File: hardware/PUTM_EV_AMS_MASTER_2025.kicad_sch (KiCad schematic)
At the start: 42 parts, among them IC11 ISO6760, IC7 ISO6760, IC8 3.3V/0.5A, J1 M80-5100642, J10 M300-MV10345M1, J12 M80-51034XX, J2 USB_C_Receptacle_USB2.0_14P, J3 M80-51014XX, J4 FTSH-107-01-L-D-K, J5 M80-51004XX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

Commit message: layotu done, some more routing done
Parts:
- removed TP1: TestPoint_Small, TestPoint:TestPoint_THTPad_D1.0mm_Drill0.5mm, symbol Connector:TestPoint_Small
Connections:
- net Isolated ADC/CAR_I: now also J8.2 (Pin_2); no longer J8.1 (Pin_1)
- net Isolated ADC/CAR_I_REF: now also J8.1 (Pin_1); no longer J8.2 (Pin_2)
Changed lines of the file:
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@@
 	)
 	(symbol
-		(lib_id "Connector:TestPoint_Small")
-		(at 45.72 54.61 0)
-		(unit 1)
-		(exclude_from_sim no)
-		(in_bom yes)
-		(on_board yes)
-		(dnp no)
-		(property "Reference" "TP1"
-			(at 43.18 54.61 0)
-			(effects
-				(font
-					(size 1.27 1.27)
-				)
-				(justify right)
-			)
-		)
-		(property "Value" "TestPoint_Small"
-			(at 46.99 55.8799 0)
-			(effects
-				(font
-					(size 1.27 1.27)
-				)
-				(justify left)
-				(hide yes)
-			)
-		)
-		(property "Footprint" "TestPoint:TestPoint_THTPad_D1.0mm_Drill0.5mm"
-			(at 50.8 54.61 0)
-			(effects
-				(font
-					(size 1.27 1.27)
-				)
-				(hide yes)
-			)
-		)
-		(property "Datasheet" "~"
-			(at 50.8 54.61 0)
-			(effects
-				(font
-					(size 1.27 1.27)
-				)
-				(hide yes)
-			)
-		)
-		(property "Description" "test point"
-			(at 45.72 54.61 0)
-			(effects
-				(font
-					(size 1.27 1.27)
-				)
-				(hide yes)
-			)
-		)
-		(pin "1"
-		)
-		(instances
-			(project ""
-				(path "/b456cffc-d9d7-4c91-91f2-36ec9a65dd1b"
-					(reference "TP1")
-					(unit 1)
-				)
-			)
-		)
-	)
-	(symbol
 		(lib_name "GND_28")
 		(lib_id "power:GND")
@@
 		)
 		(pin "CAR_I" input
-			(at 74.93 133.35 180)
+			(at 74.93 135.89 180)
 			(effects
 				(font
@@
 		)
 		(pin "CAR_I_REF" input
-			(at 74.93 135.89 180)
+			(at 74.93 133.35 180)
 			(effects
 				(font

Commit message: routing done, drc checked
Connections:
- net AIR_P_DETECTION: now also J12.21 (Pin_21); no longer J12.24 (Pin_24)
- net EXT_MOSI: now also J12.12 (Pin_12); no longer J12.13 (Pin_13)
- net EXT_SCK: now also J12.13 (Pin_13); no longer J12.12 (Pin_12)
- net GND: now also J12.2 (Pin_2)
- net TSMS: no longer J12.18 (Pin_18)
- no-connect marks 23 -> 21

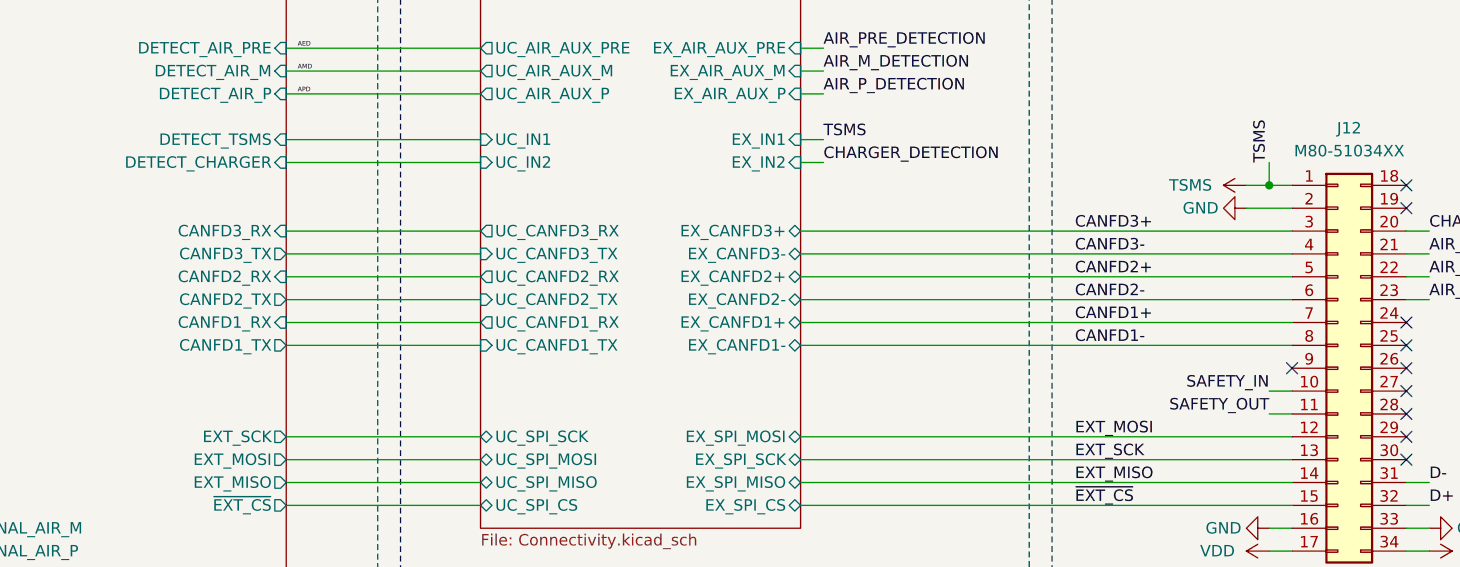
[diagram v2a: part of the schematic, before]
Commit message: changing mcu done + new routing
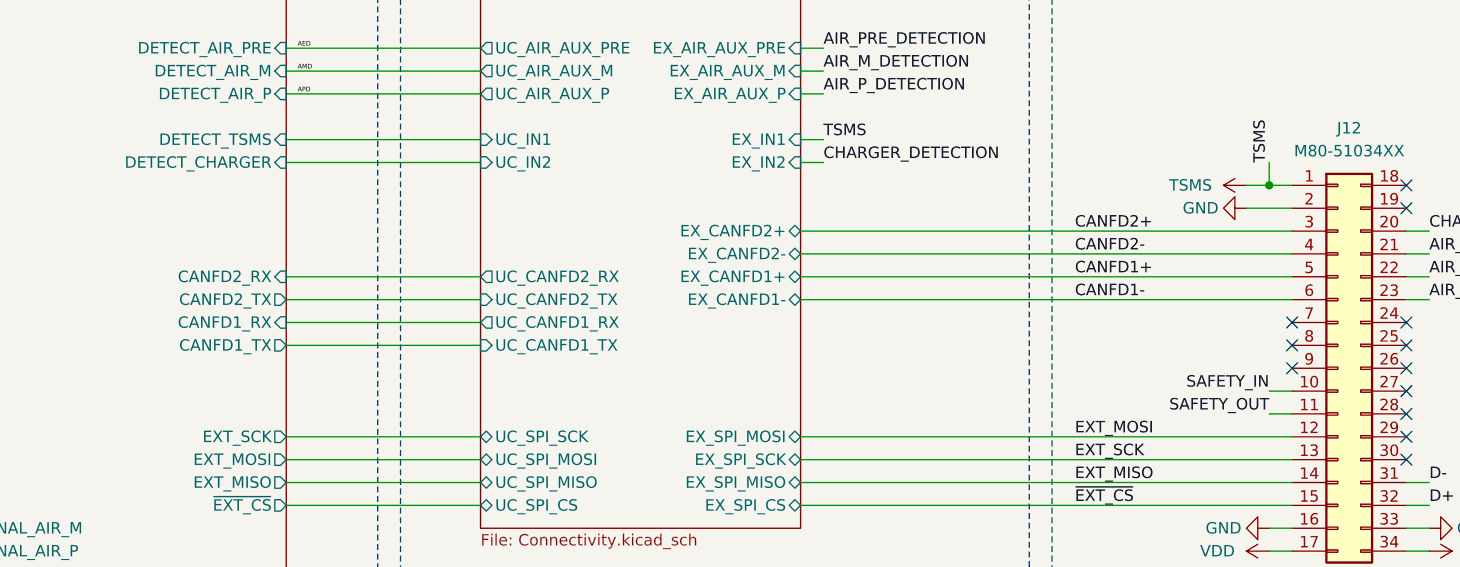
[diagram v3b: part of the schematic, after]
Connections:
- net CANFD3+ is gone; now on net CANFD2+: J12.3 (Pin_3)
- net CANFD3- is gone; now on net CANFD2-: J12.4 (Pin_4)
- net CANFD1+: now also J12.5 (Pin_5); no longer J12.7 (Pin_7)
- net CANFD1-: now also J12.6 (Pin_6); no longer J12.8 (Pin_8)
- net CANFD2+: no longer J12.5 (Pin_5)
- net CANFD2-: no longer J12.6 (Pin_6)
- no-connect marks 21 -> 23
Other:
- sheet Connectivity ports: added none; removed EX_CANFD3+, EX_CANFD3-, UC_CANFD3_RX, UC_CANFD3_TX
- sheet MCU ports: added none; removed CANFD3_RX, CANFD3_TX
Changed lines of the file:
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@@
 	)
 	(no_connect
+		(at 361.95 210.82)
+	)
+	(no_connect
+		(at 361.95 213.36)
+	)
+	(no_connect
 		(at 361.95 215.9)
 	)
@@
 	(wire
 		(pts
+			(xy 307.34 208.28) (xy 361.95 208.28)
+		)
+		(stroke
+			(width 0)
+			(type default)
+		)
+	)
+	(wire
+		(pts
 			(xy 250.19 106.68) (xy 327.66 106.68)
 		)
@@
 	(wire
 		(pts
+			(xy 307.34 200.66) (xy 361.95 200.66)
+		)
+		(stroke
+			(width 0)
+			(type default)
+		)
+	)
+	(wire
+		(pts
 			(xy 38.1 262.89) (xy 35.56 262.89)
 		)
@@
 	(wire
 		(pts
+			(xy 307.34 205.74) (xy 361.95 205.74)
+		)
+		(stroke
+			(width 0)
+			(type default)
+		)
+	)
+	(wire
+		(pts
 			(xy 114.3 238.76) (xy 114.3 267.97)
 		)
@@
 	(wire
 		(pts
-			(xy 307.34 210.82) (xy 361.95 210.82)
-		)
-		(stroke
-			(width 0)
-			(type default)
-		)
-	)
-	(wire
-		(pts
 			(xy 208.28 81.28) (xy 213.36 81.28)
 		)
@@
 	(wire
 		(pts
-			(xy 307.34 208.28) (xy 361.95 208.28)
-		)
-		(stroke
-			(width 0)
-			(type default)
-		)
-	)
-	(wire
-		(pts
 			(xy 250.19 93.98) (xy 375.92 93.98)
 		)
@@
 	(wire
 		(pts
-			(xy 307.34 205.74) (xy 361.95 205.74)
-		)
-		(stroke
-			(width 0)
-			(type default)
-		)
-	)
-	(wire
-		(pts
 			(xy 179.07 62.23) (xy 181.61 62.23)
 		)
@@
 		)
 	)
-	(wire
-		(pts
-			(xy 250.19 203.2) (xy 271.78 203.2)
-		)
-		(stroke
-			(width 0)
-			(type default)
-		)
-	)
 	(polyline
 		(pts
@@
 	(wire
 		(pts
-			(xy 307.34 200.66) (xy 361.95 200.66)
-		)
-		(stroke
-			(width 0)
-			(type default)
-		)
-	)
-	(wire
-		(pts
 			(xy 250.19 99.06) (xy 267.97 99.06)
 		)
@@
 		)
 	)
-	(wire
-		(pts
-			(xy 307.34 203.2) (xy 361.95 203.2)
-		)
-		(stroke
-			(width 0)
-			(type default)
-		)
-	)
 	(polyline
 		(pts
@@
 	(wire
 		(pts
-			(xy 48.26 114.3) (xy 74.93 114.3)
+			(xy 307.34 203.2) (xy 361.95 203.2)
 		)
 		(stroke
@@
 	(wire
 		(pts
-			(xy 107.95 172.72) (xy 125.73 172.72)
+			(xy 48.26 114.3) (xy 74.93 114.3)
 		)
 		(stroke
@@
 	(wire
 		(pts
-			(xy 392.43 31.75) (xy 392.43 39.37)
+			(xy 107.95 172.72) (xy 125.73 172.72)
 		)
 		(stroke
@@
 	(wire
 		(pts
-			(xy 85.09 41.91) (xy 85.09 44.45)
+			(xy 392.43 31.75) (xy 392.43 39.37)
 		)
 		(stroke
@@
 	(wire
 		(pts
-			(xy 307.34 226.06) (xy 361.95 226.06)
+			(xy 85.09 41.91) (xy 85.09 44.45)
 		)
 		(stroke
@@
 	(wire
 		(pts
-			(xy 85.09 52.07) (xy 85.09 54.61)
+			(xy 307.34 226.06) (xy 361.95 226.06)
 		)
 		(stroke
@@
 	(wire
 		(pts
-			(xy 250.19 200.66) (xy 271.78 200.66)
+			(xy 85.09 52.07) (xy 85.09 54.61)
 		)
 		(stroke
@@
 		)
 	)
-	(wire
-		(pts
-			(xy 307.34 213.36) (xy 361.95 213.36)
-		)
-		(stroke
-			(width 0)
-			(type default)
-		)
-	)
 	(rectangle
 		(start 157.48 242.57)
@@
 	)
 	(label "CANFD2-"
-		(at 337.82 208.28 0)
+		(at 337.82 203.2 0)
 		(fields_autoplaced yes)
 		(effects
@@
 		)
 	)
-	(label "CANFD3+"
-		(at 337.82 200.66 0)
-		(fields_autoplaced yes)
-		(effects
-			(font
-				(size 1.27 1.27)
-			)
-			(justify left bottom)
-		)
-	)
 	(label "AMD"
 		(at 251.46 182.88 0)
@@
 		)
 	)
-	(label "CANFD3-"
-		(at 337.82 203.2 0)
-		(fields_autoplaced yes)
-		(effects
-			(font
-				(size 1.27 1.27)
-			)
-			(justify left bottom)
-		)
-	)
 	(label "CCO+"
 		(at 44.45 172.72 180)
@@
 	)
 	(label "CANFD1+"
-		(at 337.82 210.82 0)
+		(at 337.82 205.74 0)
 		(fields_autoplaced yes)
 		(effects
@@
 	)
 	(label "CANFD1-"
-		(at 337.82 213.36 0)
+		(at 337.82 208.28 0)
 		(fields_autoplaced yes)
 		(effects
@@
 	)
 	(label "CANFD2+"
-		(at 337.82 205.74 0)
+		(at 337.82 200.66 0)
 		(fields_autoplaced yes)
 		(effects
@@
 			)
 		)
-		(pin "DETECT_CHARGER" input
-			(at 250.19 193.04 0)
-			(effects
-				(font
-					(size 1.27 1.27)
-				)
-				(justify right)
-			)
-		)
 		(pin "DETECT_AIR_P" input
 			(at 250.19 185.42 0)
@@
 			)
 		)
-		(pin "DETECT_TSMS" input
-			(at 250.19 190.5 0)
-			(effects
-				(font
-					(size 1.27 1.27)
-				)
-				(justify right)
-			)
-		)
 		(pin "SIGNAL_AIR_M" output
 			(at 213.36 233.68 180)
@@
 			)
 		)
-		(pin "CANFD3_RX" input
-			(at 250.19 200.66 0)
-			(effects
-				(font
-					(size 1.27 1.27)
-				)
-				(justify right)
-			)
-		)
-		(pin "CANFD3_TX" output
-			(at 250.19 203.2 0)
-			(effects
-				(font
-					(size 1.27 1.27)
-				)
-				(justify right)
-			)
-		)
 		(pin "DETECT_WTDG" input
 			(at 213.36 81.28 180)
@@
 			)
 		)
+		(pin "DETECT_CHARGER" input
+			(at 250.19 193.04 0)
+			(effects
+				(font
+					(size 1.27 1.27)
+				)
+				(justify right)
+			)
+		)
+		(pin "DETECT_TSMS" input
+			(at 250.19 190.5 0)
+			(effects
+				(font
+					(size 1.27 1.27)
+				)
+				(justify right)
+			)
+		)
 		(instances
 			(project "PUTM_EV_AMS_MASTER_2025"
@@
 			)
 		)
-		(pin "EX_CANFD3-" bidirectional
-			(at 307.34 203.2 0)
-			(effects
-				(font
-					(size 1.27 1.27)
-				)
-				(justify right)
-			)
-		)
-		(pin "EX_CANFD3+" bidirectional
-			(at 307.34 200.66 0)
-			(effects
-				(font
-					(size 1.27 1.27)
-				)
-				(justify right)
-			)
-		)
-		(pin "UC_CANFD3_RX" output
-			(at 271.78 200.66 180)
-			(effects
-				(font
-					(size 1.27 1.27)
-				)
-				(justify left)
-			)
-		)
-		(pin "UC_CANFD3_TX" input
-			(at 271.78 203.2 180)
-			(effects
-				(font
-					(size 1.27 1.27)
-				)
-				(justify left)
-			)
-		)
 		(pin "EX_IN1" input
 			(at 307.34 190.5 0)
@@
 		)
 		(pin "EX_CANFD1-" bidirectional
-			(at 307.34 213.36 0)
+			(at 307.34 208.28 0)
 			(effects
 				(font
@@
 		)
 		(pin "EX_CANFD1+" bidirectional
-			(at 307.34 210.82 0)
+			(at 307.34 205.74 0)
 			(effects
 				(font
@@
 		)
 		(pin "EX_CANFD2+" bidirectional
-			(at 307.34 205.74 0)
+			(at 307.34 200.66 0)
 			(effects
 				(font
@@
 		)
 		(pin "EX_CANFD2-" bidirectional
-			(at 307.34 208.28 0)
+			(at 307.34 203.2 0)
 			(effects
 				(font

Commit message: sync
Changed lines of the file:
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@@
 	(wire
 		(pts
-			(xy 250.19 210.82) (xy 271.78 210.82)
+			(xy 250.19 205.74) (xy 271.78 205.74)
 		)
 		(stroke
@@
 	(wire
 		(pts
-			(xy 250.19 213.36) (xy 271.78 213.36)
+			(xy 250.19 208.28) (xy 271.78 208.28)
 		)
 		(stroke
@@
 	(wire
 		(pts
-			(xy 250.19 208.28) (xy 271.78 208.28)
+			(xy 250.19 203.2) (xy 271.78 203.2)
 		)
 		(stroke
@@
 	(wire
 		(pts
-			(xy 250.19 205.74) (xy 271.78 205.74)
+			(xy 250.19 200.66) (xy 271.78 200.66)
 		)
 		(stroke
@@
 		)
 		(pin "CANFD1_RX" input
-			(at 250.19 210.82 0)
+			(at 250.19 205.74 0)
 			(effects
 				(font
@@
 		)
 		(pin "CANFD2_TX" output
-			(at 250.19 208.28 0)
+			(at 250.19 203.2 0)
 			(effects
 				(font
@@
 		)
 		(pin "CANFD2_RX" input
-			(at 250.19 205.74 0)
+			(at 250.19 200.66 0)
 			(effects
 				(font
@@
 		)
 		(pin "CANFD1_TX" output
-			(at 250.19 213.36 0)
+			(at 250.19 208.28 0)
 			(effects
 				(font
@@
 		)
 		(pin "UC_CANFD1_RX" output
-			(at 271.78 210.82 180)
+			(at 271.78 205.74 180)
 			(effects
 				(font
@@
 		)
 		(pin "UC_CANFD1_TX" input
-			(at 271.78 213.36 180)
+			(at 271.78 208.28 180)
 			(effects
 				(font
@@
 		)
 		(pin "UC_CANFD2_TX" input
-			(at 271.78 208.28 180)
+			(at 271.78 203.2 180)
 			(effects
 				(font
@@
 		)
 		(pin "UC_CANFD2_RX" output
-			(at 271.78 205.74 180)
+			(at 271.78 200.66 180)
 			(effects
 				(font

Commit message: sync;
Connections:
- net D+: no longer J12.32 (Pin_32)
- net D-: no longer J12.31 (Pin_31)
- net CC_D-: now reaches J12.7 (Pin_7)
- net CC_D+: now reaches J12.8 (Pin_8)
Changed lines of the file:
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@@
 	)
 	(no_connect
+		(at 374.65 228.6)
+	)
+	(no_connect
 		(at 374.65 213.36)
 	)
@@
 	)
 	(no_connect
-		(at 361.95 210.82)
-	)
-	(no_connect
-		(at 361.95 213.36)
-	)
-	(no_connect
 		(at 361.95 215.9)
 	)
@@
 	)
 	(no_connect
+		(at 374.65 231.14)
+	)
+	(no_connect
 		(at 375.92 76.2)
 	)
@@
 		)
 	)
+	(wire
+		(pts
+			(xy 307.34 139.7) (xy 309.88 139.7)
+		)
+		(stroke
+			(width 0)
+			(type default)
+		)
+	)
 	(polyline
 		(pts
@@
 	(wire
 		(pts
+			(xy 361.95 210.82) (xy 359.41 210.82)
+		)
+		(stroke
+			(width 0)
+			(type default)
+		)
+	)
+	(wire
+		(pts
 			(xy 307.34 180.34) (xy 309.88 180.34)
 		)
@@
 	(wire
 		(pts
+			(xy 361.95 213.36) (xy 359.41 213.36)
+		)
+		(stroke
+			(width 0)
+			(type default)
+		)
+	)
+	(wire
+		(pts
 			(xy 307.34 193.04) (xy 309.88 193.04)
 		)
@@
 	(wire
 		(pts
-			(xy 186.69 49.53) (xy 186.69 52.07)
+			(xy 307.34 142.24) (xy 309.88 142.24)
 		)
 		(stroke
@@
 	(wire
 		(pts
-			(xy 375.92 93.98) (xy 375.92 91.44)
+			(xy 186.69 49.53) (xy 186.69 52.07)
 		)
 		(stroke
@@
 	(wire
 		(pts
-			(xy 181.61 59.69) (xy 179.07 59.69)
+			(xy 375.92 93.98) (xy 375.92 91.44)
 		)
 		(stroke
@@
 	(wire
 		(pts
-			(xy 115.57 109.22) (xy 115.57 165.1)
+			(xy 181.61 59.69) (xy 179.07 59.69)
 		)
 		(stroke
@@
 	(wire
 		(pts
-			(xy 195.58 256.54) (xy 213.36 256.54)
+			(xy 115.57 109.22) (xy 115.57 165.1)
 		)
 		(stroke
@@
 	(wire
 		(pts
-			(xy 392.43 29.21) (xy 392.43 31.75)
+			(xy 195.58 256.54) (xy 213.36 256.54)
 		)
 		(stroke
@@
 	(wire
 		(pts
-			(xy 374.65 231.14) (xy 377.19 231.14)
+			(xy 392.43 29.21) (xy 392.43 31.75)
 		)
 		(stroke
@@
 	(wire
 		(pts
-			(xy 374.65 228.6) (xy 377.19 228.6)
-		)
-		(stroke
-			(width 0)
-			(type default)
-		)
-	)
-	(wire
-		(pts
 			(xy 39.37 175.26) (xy 45.72 175.26)
 		)
@@
 		)
 	)
-	(label "D+"
-		(at 377.19 231.14 0)
-		(fields_autoplaced yes)
-		(effects
-			(font
-				(size 1.27 1.27)
-			)
-			(justify left bottom)
-		)
-	)
 	(label "SIGNAL_LED_3"
 		(at 370.84 39.37 180)
@@
 		)
 	)
+	(label "FC3"
+		(at 212.09 259.08 180)
+		(fields_autoplaced yes)
+		(effects
+			(font
+				(size 0.508 0.508)
+			)
+			(justify right bottom)
+		)
+	)
 	(label "ISO_ADC_MOSI"
 		(at 147.32 96.52 180)
@@
 		)
 	)
+	(label "D+"
+		(at 309.88 142.24 0)
+		(fields_autoplaced yes)
+		(effects
+			(font
+				(size 1.27 1.27)
+			)
+			(justify left bottom)
+		)
+	)
+	(label "FC4"
+		(at 212.09 261.62 180)
+		(fields_autoplaced yes)
+		(effects
+			(font
+				(size 0.508 0.508)
+			)
+			(justify right bottom)
+		)
+	)
 	(label "AIR_M_DETECTION"
 		(at 377.19 208.28 0)
@@
 		)
 	)
+	(label "CRX2"
+		(at 251.46 200.66 0)
+		(fields_autoplaced yes)
+		(effects
+			(font
+				(size 0.508 0.508)
+			)
+			(justify left bottom)
+		)
+	)
 	(label "FAN1-"
 		(at 142.24 254 0)
@@
 		)
 	)
+	(label "CTX2"
+		(at 251.46 203.2 0)
+		(fields_autoplaced yes)
+		(effects
+			(font
+				(size 0.508 0.508)
+			)
+			(justify left bottom)
+		)
+	)
 	(label "UART_RX"
 		(at 358.14 93.98 180)
@@
 		)
 	)
+	(label "FC7"
+		(at 212.09 269.24 180)
+		(fields_autoplaced yes)
+		(effects
+			(font
+				(size 0.508 0.508)
+			)
+			(justify right bottom)
+		)
+	)
 	(label "SAE"
 		(at 212.09 238.76 180)
@@
 		)
 	)
+	(label "D-"
+		(at 309.88 139.7 0)
+		(fields_autoplaced yes)
+		(effects
+			(font
+				(size 1.27 1.27)
+			)
+			(justify left bottom)
+		)
+	)
 	(label "~{EXT_CS}"
 		(at 337.82 231.14 0)
@@
 		)
 	)
+	(label "FC1"
+		(at 212.09 254 180)
+		(fields_autoplaced yes)
+		(effects
+			(font
+				(size 0.508 0.508)
+			)
+			(justify right bottom)
+		)
+	)
+	(label "CRX1"
+		(at 251.46 205.74 0)
+		(fields_autoplaced yes)
+		(effects
+			(font
+				(size 0.508 0.508)
+			)
+			(justify left bottom)
+		)
+	)
+	(label "CC_D-"
+		(at 359.41 210.82 180)
+		(fields_autoplaced yes)
+		(effects
+			(font
+				(size 1.27 1.27)
+			)
+			(justify right bottom)
+		)
+	)
 	(label "LED3"
 		(at 383.54 39.37 180)
@@
 		)
 	)
+	(label "T"
+		(at 251.46 190.5 0)
+		(fields_autoplaced yes)
+		(effects
+			(font
+				(size 0.508 0.508)
+			)
+			(justify left bottom)
+		)
+	)
 	(label "CCO+"
 		(at 44.45 172.72 180)
@@
 		)
 	)
+	(label "FC5"
+		(at 212.09 264.16 180)
+		(fields_autoplaced yes)
+		(effects
+			(font
+				(size 0.508 0.508)
+			)
+			(justify right bottom)
+		)
+	)
 	(label "AIR_PRE_DETECTION"
 		(at 377.19 205.74 0)
@@
 		)
 	)
+	(label "~{ECS}"
+		(at 251.46 231.14 0)
+		(fields_autoplaced yes)
+		(effects
+			(font
+				(size 0.508 0.508)
+			)
+			(justify left bottom)
+		)
+	)
+	(label "CC_D+"
+		(at 359.41 213.36 180)
+		(fields_autoplaced yes)
+		(effects
+			(font
+				(size 1.27 1.27)
+			)
+			(justify right bottom)
+		)
+	)
 	(label "SAM"
 		(at 212.09 233.68 180)
@@
 		)
 	)
+	(label "EMI"
+		(at 251.46 228.6 0)
+		(fields_autoplaced yes)
+		(effects
+			(font
+				(size 0.508 0.508)
+			)
+			(justify left bottom)
+		)
+	)
 	(label "~{ISO_ADC_CS}"
 		(at 147.32 101.6 180)
@@
 		)
 	)
-	(label "D-"
-		(at 377.19 228.6 0)
+	(label "EXT_MOSI"
+		(at 337.82 223.52 0)
 		(fields_autoplaced yes)
 		(effects
@@
 		)
 	)
-	(label "EXT_MOSI"
-		(at 337.82 223.52 0)
+	(label "CD"
+		(at 251.46 193.04 0)
 		(fields_autoplaced yes)
 		(effects
 			(font
-				(size 1.27 1.27)
+				(size 0.508 0.508)
 			)
 			(justify left bottom)
@@
 		)
 	)
+	(label "EMO"
+		(at 251.46 223.52 0)
+		(fields_autoplaced yes)
+		(effects
+			(font
+				(size 0.508 0.508)
+			)
+			(justify left bottom)
+		)
+	)
 	(label "F_+3VISO"
 		(at 52.07 44.45 180)
@@
 		)
 	)
+	(label "ESC"
+		(at 251.46 226.06 0)
+		(fields_autoplaced yes)
+		(effects
+			(font
+				(size 0.508 0.508)
+			)
+			(justify left bottom)
+		)
+	)
 	(label "ISO_ADC_MISO"
 		(at 147.32 148.59 180)
@@
 		)
 	)
+	(label "FC6"
+		(at 212.09 266.7 180)
+		(fields_autoplaced yes)
+		(effects
+			(font
+				(size 0.508 0.508)
+			)
+			(justify right bottom)
+		)
+	)
+	(label "CTX1"
+		(at 251.46 208.28 0)
+		(fields_autoplaced yes)
+		(effects
+			(font
+				(size 0.508 0.508)
+			)
+			(justify left bottom)
+		)
+	)
 	(label "NRST"
 		(at 358.14 88.9 180)
@@
 		)
 	)
+	(label "FC2"
+		(at 212.09 256.54 180)
+		(fields_autoplaced yes)
+		(effects
+			(font
+				(size 0.508 0.508)
+			)
+			(justify right bottom)
+		)
+	)
 	(symbol
 		(lib_id "Device:R_Small")
@@
 		)
 		(pin "EX_D-" bidirectional
-			(at 307.34 133.35 0)
+			(at 307.34 139.7 0)
 			(effects
 				(font
@@
 		)
 		(pin "EX_D+" bidirectional
-			(at 307.34 135.89 0)
+			(at 307.34 142.24 0)
 			(effects
 				(font
